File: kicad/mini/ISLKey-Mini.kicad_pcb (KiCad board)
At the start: 2 copper layers, 60 x 60 mm, 25 parts, among them J1 12V AC/DC IN, J2 LOCK COM/NO/NC, J3 EXIT, K1 G6E (2A), M1 TTGO T-Display, Q1 MMBT2222A, U2 AP63203WU

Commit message: mini: add 8mm hole above the TTGO + re-route
8mm Edge.Cuts cutout, horizontally centred at (30,28) - just above the TTGO,
slightly above board-centre. Moved D3/R4 clear of it; re-routed around the
hole (171 traces + 4 vias, 0 unconnected); GND pours auto-clip to the cutout.

Co-Authored-By: Claude Opus 4.8 <noreply@anthropic.com>
Claude-Session: https://claude.ai/code/session_01WaJbCVpNNC7xF4fkqWpjpA
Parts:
- moved R4 13.2 mm to (19.7, 28.0)
- moved D3 7.07 mm to (19.7, 25.0)
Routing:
- net GND: track 157.4 -> 171.9 mm, vias 1 -> 0
- net +3V3: track 72.9 -> 61.6 mm
- net FB: track 34.7 -> 23.7 mm
- net +5V: track 119.6 -> 130.4 mm, vias 0 -> 2
- net ACL: track 32.7 -> 42.0 mm, vias 1 -> 0
- net RLY: track 59.0 -> 63.6 mm
- net D3K: track 6.82 -> 2.96 mm
- net LK_NC: track 29.3 -> 33.1 mm
- net LK_COM: track 26.2 -> 24.2 mm
- net RAWP: track 30.5 -> 29.1 mm
- net ACN: track 28.5 -> 27.3 mm
- net RLY_B: track 16.8 -> 15.6 mm
- net K_C: track 33.5 -> 33.9 mm, vias 0 -> 1
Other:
- outline, holes or cut-outs redrawn

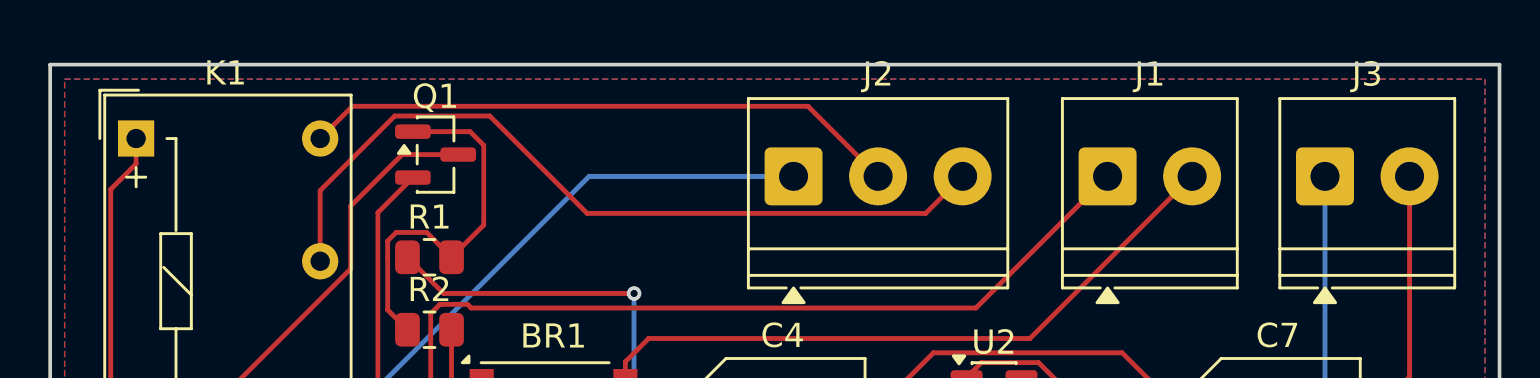
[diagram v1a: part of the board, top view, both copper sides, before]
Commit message: mini: terminal silk labels + PCBWay package
Silk labels 12V/LOCK/EXIT on the terminals (+ RELAY). Full PCBWay package:
gerbers + drill + paste + CPL + BOM + turnkey BOM (MPNs) + fab readme noting
the 1-gang screw notches and 8mm cutout. Zipped to ISLKey-Mini-PCBWay.zip.

Co-Authored-By: Claude Opus 4.8 <noreply@anthropic.com>
Claude-Session: https://claude.ai/code/session_01WaJbCVpNNC7xF4fkqWpjpA
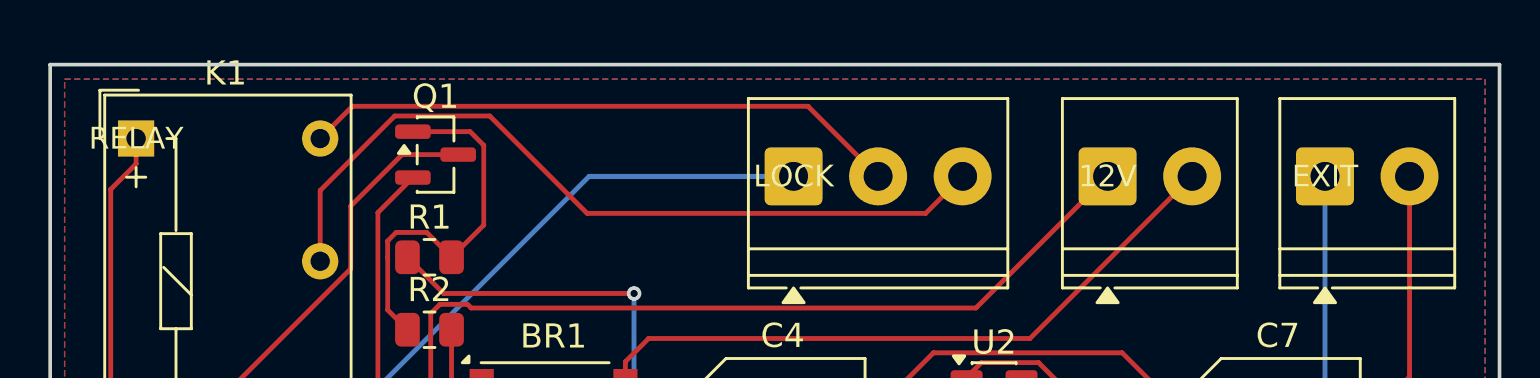
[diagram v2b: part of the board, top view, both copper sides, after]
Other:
- board text added: "12V"
- board text added: "EXIT"
- board text added: "LOCK"
- board text added: "RELAY"
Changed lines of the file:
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@@
 			(at 3.5 -4.22 0)
 			(layer "F.SilkS")
+			(hide yes)
 			(effects
 				(font
@@
 			(at 1.75 -4.22 0)
 			(layer "F.SilkS")
+			(hide yes)
 			(effects
 				(font
@@
 			(at 1.75 -4.22 0)
 			(layer "F.SilkS")
+			(hide yes)
 			(effects
 				(font
@@
 		(layer "Edge.Cuts")
 	)
+	(gr_text "RELAY"
+		(at 3.56 3.06 0)
+		(layer "F.SilkS")
+		(effects
+			(font
+				(size 0.9 0.9)
+				(thickness 0.15)
+			)
+		)
+	)
+	(gr_text "LOCK"
+		(at 30.775 4.625 0)
+		(layer "F.SilkS")
+		(effects
+			(font
+				(size 0.9 0.9)
+				(thickness 0.15)
+			)
+		)
+	)
+	(gr_text "12V"
+		(at 43.775 4.625 0)
+		(layer "F.SilkS")
+		(effects
+			(font
+				(size 0.9 0.9)
+				(thickness 0.15)
+			)
+		)
+	)
+	(gr_text "EXIT"
+		(at 52.775 4.625 0)
+		(layer "F.SilkS")
+		(effects
+			(font
+				(size 0.9 0.9)
+				(thickness 0.15)
+			)
+		)
+	)
 	(segment

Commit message: mini: add ISL logo + back silk text; regenerate PCBWay package
- Board (1-MINI, V2.0.0): user-placed 12mm ISL logo footprint on the
  back silk plus back text ("1-Mini" + company line).
- Regenerated the full PCBWay package from the edited board with zones
  refilled and silk-over-mask clipping: 9 .gbr layers, PTH+NPTH drill,
  gerber job file. Back silkscreen now contains the logo + text.
- Verified pre-ship: 0 unconnected pads (fully routed); schematic net
  parity clean except the TTGO's unused GPIO pins (floating by design);
  no electrical/clearance/short DRC. Remaining flags are cosmetic silk.
- Untrack scratch (drc.txt, .kicad_prl); ignore .lck and stray
  project-folder footprint copies.

Co-Authored-By: Claude Opus 4.8 <noreply@anthropic.com>
Claude-Session: https://claude.ai/code/session_01WaJbCVpNNC7xF4fkqWpjpA
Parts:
- added G***: LOGO, ISLKey:logo 12mm, F.Cu at (11.5, 28.5)
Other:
- board text added: "1-Mini"
- board text added: "A THE SAPPHIRE MARCEL GROUP company"
